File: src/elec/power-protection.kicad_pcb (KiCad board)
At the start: 2 copper layers, 10.2 x 20.2 mm, 12 parts, among them J1 Conn_01x03_Pin, Q1 BSS138, Q2 BSS138, Q3 BC857, Q4 BC857

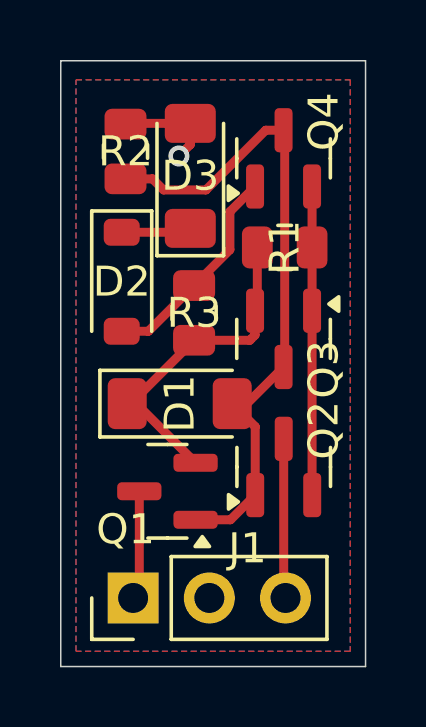
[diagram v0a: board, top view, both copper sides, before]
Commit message: Fix: wrong MOSFET (p channel needed); README.md added
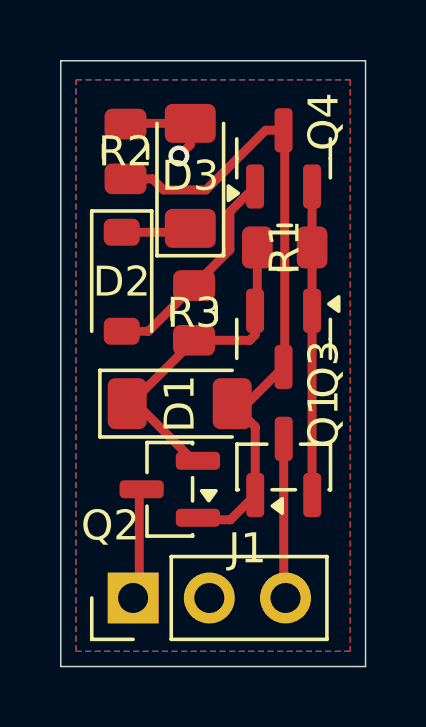
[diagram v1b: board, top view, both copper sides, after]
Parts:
- Q1, Q2: value BSS138 -> BSS83P
- moved Q1 3.96 mm to (128.8, 80.7), turned to 90 degrees
- moved Q2 3.87 mm to (125.0, 81.5), turned to 180 degrees
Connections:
- Q1 pad 2: Net-(D1-K) -> Net-(Q1-S)
- Q1 pad 3: Net-(J1-Pin_1) -> Net-(J1-Pin_3)
- Q2 pad 2: Net-(Q2-S) -> Net-(D1-K)
- Q2 pad 3: Net-(J1-Pin_3) -> Net-(J1-Pin_1)
- Q3 pad 1: Net-(Q2-S) -> Net-(Q1-S)
- Q4 pad 2: Net-(Q2-S) -> Net-(Q1-S)
- R1 pad 2: Net-(Q2-S) -> Net-(Q1-S)
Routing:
- net Net-(Q2-S): track 10.3 -> 0.00 mm
- net Net-(Q1-S): track 0.00 -> 10.3 mm
